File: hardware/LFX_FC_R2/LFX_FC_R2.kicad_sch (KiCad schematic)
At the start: 0 parts

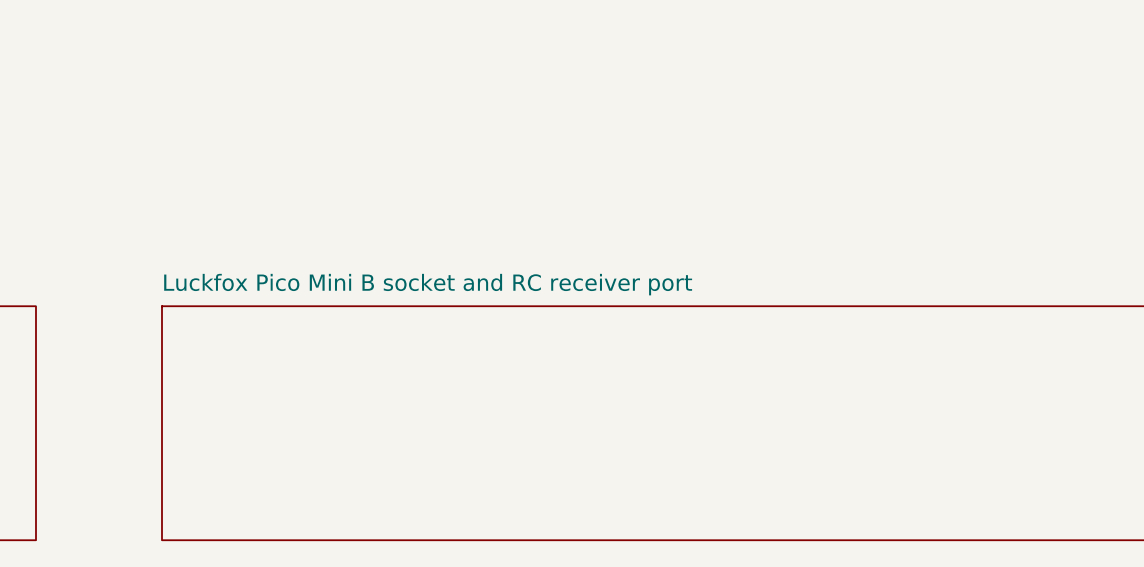
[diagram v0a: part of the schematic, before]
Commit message: hardware: LFX_FC_R2 GPS port J18 (ATGM336H / NEO-M8N class) on UART5
- J18: JST-SH 4-pin at the left edge, 1 +5V, 2 GND, 3 NC, 4 module TXD ->
  board RX.  MOD1 pin 14 (GPIO1_D2) becomes UART5_RX_M1, 33R + TPD1E05U06 ESD.
- Baro chip select moves to pin 15 (GPIO1_D3, MCU GPIO); IMU INT1 dropped
  (polled).
- +5V to J18 hand-routed from J4 on B.Cu along the board edge (x 0.75), so it
  walls nothing in.
- Hand routes for the connections the router kept leaving open: SIM RST/CLK
  (U12 channels swapped so they no longer cross), BUZ_CTRL, the U2 +5V
  escape, LTE_1V8 between U9/U10 (paths taken from dc53508).
- gen_sch keeps the board rules in kicad_pro; clean_stubs removes dangling
  vias; Freerouting runs as a background UI element on macOS.
- DRC: 0 violations, 0 unconnected, schematic parity clean; ERC 0.

Co-Authored-By: Claude Opus 5.5 <noreply@anthropic.com>
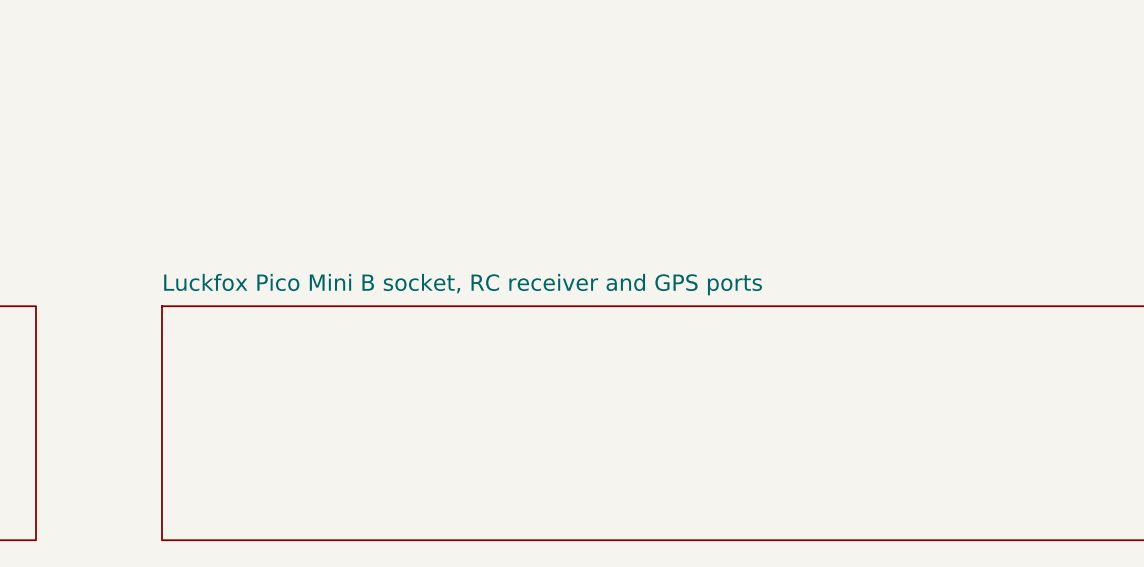
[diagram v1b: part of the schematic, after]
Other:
- sheet Luckfox Pico Mini B socket and RC receiver port renamed Luckfox Pico Mini B socket, RC receiver and GPS ports
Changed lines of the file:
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@@
 		(stroke (width 0.2) (type solid))
 		(fill (color 0 0 0 0.0))
-		(property "Sheetname" "Luckfox Pico Mini B socket and RC receiver port"
+		(property "Sheetname" "Luckfox Pico Mini B socket, RC receiver and GPS ports"
 			(at 199 68.5 0)
 			(effects (font (size 1.8 1.8)) (justify left bottom))
